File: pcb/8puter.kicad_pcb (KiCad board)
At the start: 2 copper layers, 120 x 100 mm, 44 parts, among them J1 PWR-DC, J2 DB15_Female, U2 74AHC74, U6 MAX811MEUS-T, Y1 1.8432MHz

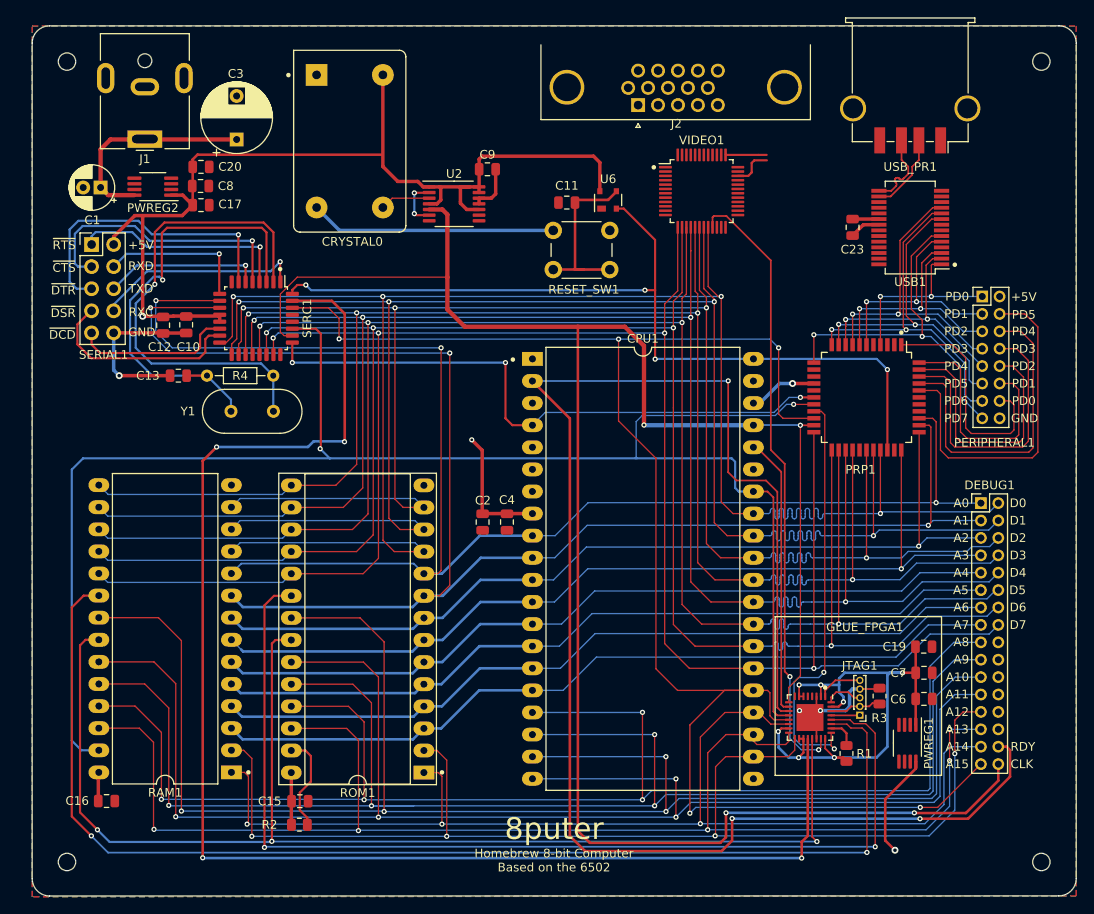
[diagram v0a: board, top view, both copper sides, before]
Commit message: Pulldowns, minor reroute
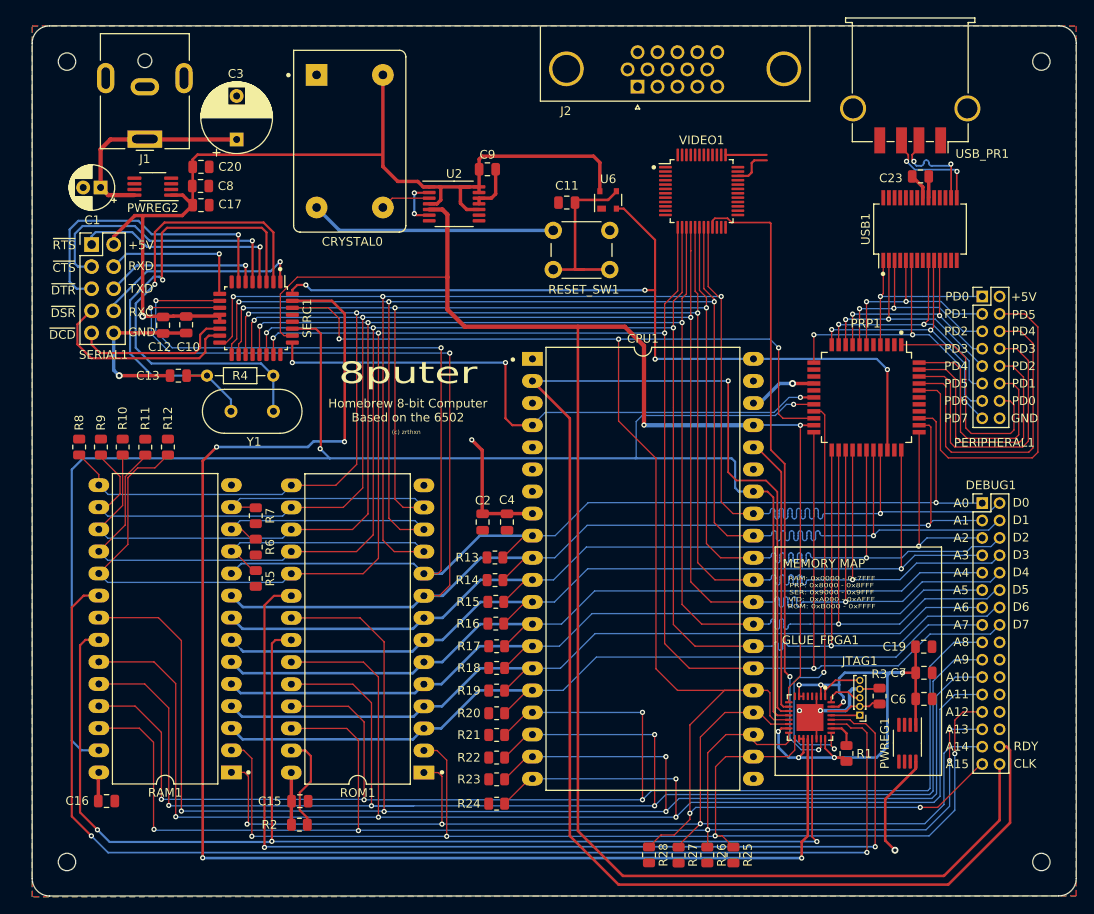
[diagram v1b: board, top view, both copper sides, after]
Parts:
- added R10: 10K, Resistor_SMD:R_0805_2012Metric, F.Cu at (99.1, 83.6)
- added R11: 10K, Resistor_SMD:R_0805_2012Metric, F.Cu at (101.7, 83.7)
- added R12: 10K, Resistor_SMD:R_0805_2012Metric, F.Cu at (104.3, 83.6)
- added R13: 10K, Resistor_SMD:R_0805_2012Metric, F.Cu at (141.9, 96.3)
- added R14: 10K, Resistor_SMD:R_0805_2012Metric, F.Cu at (141.9, 98.9)
- added R15: 10K, Resistor_SMD:R_0805_2012Metric, F.Cu at (142.0, 101.4)
- added R16: 10K, Resistor_SMD:R_0805_2012Metric, F.Cu at (142.0, 103.9)
- added R17: 10K, Resistor_SMD:R_0805_2012Metric, F.Cu at (142.1, 106.5)
- added R18: 10K, Resistor_SMD:R_0805_2012Metric, F.Cu at (142.1, 109.0)
- added R19: 10K, Resistor_SMD:R_0805_2012Metric, F.Cu at (142.1, 111.6)
- added R20: 10K, Resistor_SMD:R_0805_2012Metric, F.Cu at (142.1, 114.2)
- added R21: 10K, Resistor_SMD:R_0805_2012Metric, F.Cu at (142.1, 116.7)
- added R22: 10K, Resistor_SMD:R_0805_2012Metric, F.Cu at (142.1, 119.3)
- added R23: 10K, Resistor_SMD:R_0805_2012Metric, F.Cu at (142.1, 121.8)
- added R24: 10K, Resistor_SMD:R_0805_2012Metric, F.Cu at (142.1, 124.6)
- added R25: 10K, Resistor_SMD:R_0805_2012Metric, F.Cu at (169.3, 130.5)
- added R26: 10K, Resistor_SMD:R_0805_2012Metric, F.Cu at (166.3, 130.5)
- added R27: 10K, Resistor_SMD:R_0805_2012Metric, F.Cu at (163.0, 130.6)
- added R28: 10K, Resistor_SMD:R_0805_2012Metric, F.Cu at (159.6, 130.5)
- added R5: 10K, Resistor_SMD:R_0805_2012Metric, F.Cu at (114.4, 98.8)
- added R6: 10K, Resistor_SMD:R_0805_2012Metric, F.Cu at (114.4, 95.1)
- added R7: 10K, Resistor_SMD:R_0805_2012Metric, F.Cu at (114.4, 91.5)
- added R8: 10K, Resistor_SMD:R_0805_2012Metric, F.Cu at (94.1, 83.6)
- added R9: 10K, Resistor_SMD:R_0805_2012Metric, F.Cu at (96.6, 83.6)
- ROM1: footprint Package_DIP:DIP-28_W15.24mm_Socket_LongPads -> Package_DIP:DIP-28_W15.24mm_LongPads
- moved C23 9.75 mm to (190.8, 52.5), turned to 180 degrees
- moved J2 2.12 mm to (158.3, 42.2)
- moved USB1 1.14 mm to (190.7, 58.6), turned to 90 degrees
- moved DEBUG1 0.15 mm to (197.9, 90.1)
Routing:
- net DATA7: track 224.0 -> 242.2 mm
- net DATA6: track 217.2 -> 230.7 mm
- net DATA5: track 212.5 -> 222.3 mm
- net DATA4: track 207.3 -> 215.9 mm
- net /Peripheral Handler/PD3: track 35.0 -> 26.4 mm
- net /Peripheral Handler/PD6: track 40.5 -> 32.7 mm
- net /Peripheral Handler/PD5: track 37.9 -> 30.6 mm
- net ADDR15: track 185.0 -> 191.9 mm
- net /Peripheral Handler/PD7: track 42.8 -> 37.2 mm
- net RDY: track 180.9 -> 185.5 mm, vias 3 -> 1
- net ADDR1: track 180.1 -> 184.7 mm
- net DATA3: track 202.5 -> 207.1 mm
- net ADDR11: track 177.2 -> 181.7 mm
- net ADDR3: track 104.9 -> 109.4 mm
- net ADDR9: track 177.1 -> 181.6 mm
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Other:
- board text added: "(c) zrthxn"
- board text added: "MEMORY MAP"
- board text added: "RAM: 0x0000 - 0x7FFF PRP: 0x8000 - 0x8FFF SER: 0x9000 - 0x9FFF VID: 0xA000 - 0xAFFF ROM: 0xB000 - 0xFFFF"
- board text added: "Revision 1 | Apr 2022 Designed by A. Husain"
- board text added: "github.com/zrthxn/8puter (c) MIT Licence"
- board text removed: "Revision 1 | Apr 2022 Design by zrthxn"

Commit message: Update readme
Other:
- board text added: "github.com/zrthxn/8puter (C) GPL-3.0 License"
- board text removed: "github.com/zrthxn/8puter (c) MIT Licence"
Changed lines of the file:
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@@
     (effects (font (size 1.25 1.25) (thickness 0.25)) (justify mirror))
   )
-  (gr_text "github.com/zrthxn/8puter\n(c) MIT Licence" (at 201.398 125.645) (layer "B.SilkS")
+  (gr_text "github.com/zrthxn/8puter\n(C) GPL-3.0 License" (at 201.398 125.645) (layer "B.SilkS")
     (effects (font (size 1.25 1.25) (thickness 0.15)) (justify left mirror))
   )

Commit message: First completed routing
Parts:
- removed CRYSTAL0: ACO-10MHz-A, Oscillator:Oscillator_DIP-14_LargePads
- removed J2: DB15_Female, Connector_Dsub:DSUB-15-HD_Female_Horizontal_P2.29x1.98mm_EdgePinOffset3.03mm_Housed_MountingHolesOffset4.94mm
- removed PWREG1: LT1962-3.3, Package_SO:MSOP-8_3x3mm_P0.65mm
- removed PWREG2: LT1962-5, Package_SO:MSOP-8_3x3mm_P0.65mm
- removed USB_PR1: USB_A, Connector_USB:USB_A_TE_292303-7_Horizontal
- added C14: 10uF, Capacitor_SMD:C_0805_2012Metric, F.Cu at (144.8, 48.1)
- added C18: 1uF, Capacitor_SMD:C_0805_2012Metric, F.Cu at (142.2, 51.2)
- added C21: 100nF, Capacitor_SMD:C_0805_2012Metric, F.Cu at (176.1, 73.7)
- added C22: 100nF, Capacitor_SMD:C_0805_2012Metric, F.Cu at (186.2, 52.5)
- added C5: 10uF, Capacitor_SMD:C_0805_2012Metric, F.Cu at (187.5, 124.6)
- added CS_SEL1: Conn_02x03_Odd_Even, Connector_PinHeader_2.00mm:PinHeader_2x03_P2.00mm_Vertical, F.Cu at (133.2, 58.8)
- added D1: LED, LED_SMD:LED_0805_2012Metric, F.Cu at (100.3, 51.4)
- added R29: 4K7, Resistor_SMD:R_0805_2012Metric, F.Cu at (102.7, 51.4)
- added R30: 10K, Resistor_SMD:R_0805_2012Metric, F.Cu at (142.3, 55.4)
- added R31: 47K, Resistor_SMD:R_0805_2012Metric, F.Cu at (142.2, 53.3)
- added REG1: NCP1117ST50T3G, Package_TO_SOT_SMD:SOT-223-3_TabPin2, F.Cu at (111.7, 50.9)
- added REG2: NCP1117ST33T3G, Package_TO_SOT_SMD:SOT-223-3_TabPin2, F.Cu at (189.6, 118.7)
- added REG3: NCP1117ST33T3G, Package_TO_SOT_SMD:SOT-223-3_TabPin2, F.Cu at (155.2, 48.4)
- added STEP_SW1: PUSHBTN, Button_Switch_THT:SW_PUSH_6mm_H13mm, F.Cu at (145.2, 63.3)
- added SWD_H1: Conn_01x04, Connector_PinHeader_2.00mm:PinHeader_1x04_P2.00mm_Vertical, F.Cu at (175.1, 49.0)
- added U3: SN74LVC1G14DBV, Package_TO_SOT_SMD:SOT-23-5, F.Cu at (140.7, 45.7)
- added USB_P1: USB_A, Connector_USB:USB_A_TE_292303-7_Horizontal, F.Cu at (189.6, 42.0)
- added VGA1: DB15_Female, Connector_Dsub:DSUB-15-HD_Female_Horizontal_P2.29x1.98mm_EdgePinOffset3.03mm_Housed_MountingHolesOffset4.94mm, F.Cu at (160.0, 42.2)
- added X1: ECS-2200BX-100, Oscillator:Oscillator_DIP-8, F.Cu at (120.4, 51.2)
- C1: footprint Capacitor_THT:CP_Radial_D5.0mm_P2.00mm -> Capacitor_SMD:C_0805_2012Metric
- C17, C6: value 10uF -> 1uF
- C19: value 100nF -> 1uF
- C23: value 10uF -> 100nF
- C3: footprint Capacitor_THT:CP_Radial_D8.0mm_P5.00mm -> Capacitor_THT:CP_Radial_D5.0mm_P2.50mm
- C7, C8: value 1uF -> 100nF
- moved C19 72.0 mm to (149.2, 48.1), turned to 90 degrees
- moved C20 39.0 mm to (147.0, 48.1), turned to 90 degrees
- moved C23 29.8 mm to (161.6, 46.3), turned to 0 degrees
- moved C3 16.3 mm to (96.2, 51.2), turned to -90 degrees
- moved C9 14.9 mm to (132.3, 39.6), turned to 90 degrees
- moved C8 12.6 mm to (112.7, 41.9)
- moved C17 12.2 mm to (112.7, 44.5)
- moved C1 9.33 mm to (105.6, 51.5), turned to -90 degrees
- moved U2 8.87 mm to (134.2, 47.3), turned to 90 degrees
- moved C6 0.86 mm to (191.2, 111.7)
- moved J1 0.50 mm to (101.6, 47.7)
- moved C11 0.39 mm to (150.1, 55.9)
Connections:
- net ~{CLOCK} renamed Net-(U2-Pad2)
- C19 pad 1: +3V3 -> +3V0
- C20 pad 1: +5V -> +3V0
- C23 pad 1: +5V -> +3V0
- U2 pad 11: GND -> Net-(U2-Pad11)
- U2 pad 12: GND -> Net-(U2-Pad12)
- U2 pad 5: CLOCK -> /Clock/OSCC
- U2 pad 8: unconnected-(U2-Pad8) -> Net-(U2-Pad12)
- U2 pad 9: unconnected-(U2-Pad9) -> /Clock/STEP
- USB1 pad 12: unconnected-(USB1-Pad12) -> /Peripheral Handler/PC4
- USB1 pad 13: unconnected-(USB1-Pad13) -> /Peripheral Handler/PC0
- USB1 pad 14: unconnected-(USB1-Pad14) -> /Peripheral Handler/PC1
- USB1 pad 17: unconnected-(USB1-Pad17) -> Net-(USB1-Pad17)
- USB1 pad 19: unconnected-(USB1-Pad19) -> ~{RESET}
- USB1 pad 22: unconnected-(USB1-Pad22) -> /Peripheral Handler/PC2
- USB1 pad 23: unconnected-(USB1-Pad23) -> /Peripheral Handler/PC3
- USB1 pad 25: unconnected-(USB1-Pad25) -> GND
- USB1 pad 4: unconnected-(USB1-Pad4) -> +5V
- VIDEO1 pad 1: +5V -> +3V0
- VIDEO1 pad 11: unconnected-(VIDEO1-Pad11) -> /Video/VSYNC
- VIDEO1 pad 22: unconnected-(VIDEO1-Pad22) -> CLOCK
- VIDEO1 pad 24: +5V -> +3V0
- VIDEO1 pad 29: unconnected-(VIDEO1-Pad29) -> /Video/HSYNC
- VIDEO1 pad 34: unconnected-(VIDEO1-Pad34) -> Net-(SWD_H1-Pad2)
- VIDEO1 pad 36: +5V -> +3V0
- VIDEO1 pad 37: unconnected-(VIDEO1-Pad37) -> Net-(SWD_H1-Pad3)
- VIDEO1 pad 41: unconnected-(VIDEO1-Pad41) -> /Video/COLOR
- VIDEO1 pad 48: +5V -> +3V0
- VIDEO1 pad 7: unconnected-(VIDEO1-Pad7) -> ~{RESET}
- VIDEO1 pad 9: +5V -> +3V0
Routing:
- net GND: track 70.9 -> 220.0 mm, vias 3 -> 22
- net +5V: track 162.2 -> 257.1 mm, vias 4 -> 5
- net +3V0: track 0.00 -> 63.8 mm, vias 0 -> 2
- net ~{RESET}: track 98.7 -> 147.4 mm, vias 4 -> 7
- net /Peripheral Handler/PC3: track 29.8 -> 63.1 mm, vias 0 -> 1
- net CLOCK: track 242.2 -> 274.2 mm, vias 2 -> 3
- net /Video/VSYNC: track 0.00 -> 30.8 mm, vias 0 -> 1
- net /Video/HSYNC: track 0.00 -> 30.5 mm, vias 0 -> 1
- net /Peripheral Handler/PC2: track 33.4 -> 63.7 mm, vias 0 -> 1
- net /Peripheral Handler/PC4: track 27.1 -> 56.9 mm, vias 0 -> 1
- net /Clock/STEP: track 0.00 -> 24.9 mm, vias 0 -> 2
- net Net-(STEP_SW1-Pad1): track 0.00 -> 17.9 mm
- net /Peripheral Handler/PC0: track 40.3 -> 57.4 mm, vias 0 -> 1
- net /Peripheral Handler/PC1: track 37.1 -> 54.1 mm, vias 0 -> 1
- net /Video/COLOR: track 0.00 -> 13.2 mm, vias 0 -> 1
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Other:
- board text added: "8puter Rev 1"
- board text added: "By A. Husain. Apr 2022. github.com/zrthxn/8puter GPL-3.0 License"
- board text added: "Input Only"
- board text added: "POWER OFF before changing"
- board text removed: "8puter Homebrew Computer"
- board text removed: "Revision 1 | Apr 2022 Designed by A. Husain"
- board text removed: "github.com/zrthxn/8puter (C) GPL-3.0 License"

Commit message: Gerber Plots
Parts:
- JTAG1: footprint Connector_PinHeader_1.00mm:PinHeader_1x05_P1.00mm_Vertical -> Connector_PinHeader_2.00mm:PinHeader_1x05_P2.00mm_Vertical
- moved JTAG1 5.03 mm to (184.6, 119.4)
- moved C22 4.04 mm to (182.8, 54.6)
- moved R3 3.66 mm to (185.6, 108.6), turned to 180 degrees
- moved R1 2.67 mm to (180.4, 120.7), turned to 180 degrees
- moved R28 2.10 mm to (161.7, 130.5)
- moved R27 1.00 mm to (164.0, 130.5)
- moved R25 0.70 mm to (168.6, 130.5)
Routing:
- net GND: track 220.0 -> 253.9 mm, vias 22 -> 28
- net /TCK: track 5.93 -> 15.6 mm
- net +5V: track 257.1 -> 250.0 mm
- net +3V3: track 67.9 -> 73.5 mm
- net ADDR9: track 181.6 -> 176.7 mm
- net RDY: track 185.5 -> 189.7 mm
- net ~{RAM_CS}: track 119.6 -> 115.6 mm
- net /TMS: track 3.31 -> 7.10 mm
- net ~{ROM_CS}: track 138.3 -> 134.6 mm
- net /Peripheral Handler/PC4: track 56.9 -> 53.4 mm
- net /Peripheral Handler/PC0: track 57.4 -> 54.0 mm
- net /TDI: track 4.39 -> 7.20 mm
- net CLOCK: track 274.2 -> 276.9 mm
- net Net-(GLUE_FPGA1-Pad26): track 3.49 -> 5.56 mm
- net ADDR15: track 191.9 -> 189.9 mm
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- added copper zone on B.Cu, net GND
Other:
- board text added: "EXT"
- board text added: "FULL"
- board text added: "STEP"
- board text removed: "Input Only"
